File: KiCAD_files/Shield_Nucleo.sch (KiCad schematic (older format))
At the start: 61 parts, among them J1 Shield_nucleo_stage_outline, J2 RJ45_LED_Shielded, J3 RJ45_LED_Shielded, J4 Conn_01x02_Male, J5 Conn_01x04_Male, U1 NUCLEO-F401RE, U2 AT25xxx, U3 TCAN334GDR

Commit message: WIP: added STM32G4 symbol and footprint LQFP64
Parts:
- removed U1: NUCLEO-F401RE, Footprints:ST_NUCLEO-G474, symbol Symbols:NUCLEO-F401RE
- added U?: STM32G474RE, Package_QFP:LQFP-64_10x10mm_P0.5mm, symbol Symbols:STM32G474RE
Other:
- moved on the sheet: J4, J5, TP1, TP10, TP11, TP4, TP5, TP6, TP7, TP8, TP9

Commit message: WIP: nearly finished composant placement
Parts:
- removed J1: Shield_nucleo_stage_outline, Footprints:Shield_nucleo_outline, symbol Symbols:Shield_nucleo_stage_outline
- removed U?: STM32G474RE, Package_QFP:LQFP-64_10x10mm_P0.5mm, symbol Symbols:STM32G474RE
- added C10, C11, C13, C20, C21, C22, C25, C26, C30, C31, C32, C5, C7, C8, C9: 100nF, Capacitor_SMD:C_0805_2012Metric, symbol Device:C_Small
- added C12: 1µF, Capacitor_SMD:C_0805_2012Metric, symbol Device:C_Small
- added C14: 10nF, Capacitor_SMD:C_0805_2012Metric, symbol Device:C_Small
- added C15, C16: CP1_Small, symbol Device:CP1_Small
- added C17, C18, C27, C28: 33pF, Capacitor_SMD:C_0805_2012Metric, symbol Device:C_Small
- added C23, C33: 1uF, Capacitor_SMD:C_0805_2012Metric, symbol Device:C_Small
- added C24, C34: 10uF, Capacitor_SMD:C_1210_3225Metric, symbol Device:C_Small
- added C3, C4: 12pF, Capacitor_SMD:C_0805_2012Metric, symbol Device:C_Small
- added C6: 4,7uF, Capacitor_SMD:C_0805_2012Metric, symbol Device:C_Small
- added D10, D11: STTH4R02U, Diode_SMD:D_SMB, symbol Device:D_Schottky
- added D3, D4, D5, D6, D7, D8, D9: 3.3V, Diode_SMD:D_SOD-123, symbol Device:D_Zener_Small
- added FB1: Ferrite_Bead_Small, Resistor_SMD:R_0805_2012Metric, symbol Device:Ferrite_Bead_Small
- added J1, J6: Conn_01x02, symbol Connector_Generic:Conn_01x02
- added J7: Conn_01x03_Female, symbol Connector:Conn_01x03_Female
- added J?: Conn_02x05_Counter_Clockwise, symbol Connector_Generic:Conn_02x05_Counter_Clockwise
- added PS1: IA0505S, Converter_DCDC:Converter_DCDC_muRata_CRE1xxxxxx3C_THT, symbol Converter_DCDC:IA0505S
- added PS2: IA0512S, Converter_DCDC:Converter_DCDC_muRata_CRE1xxxxxx3C_THT, symbol Converter_DCDC:IA0512S
- added PS4: PQDE6W-Q110-S5-D, Footprints:PQDE6W-Q110-S5-D, symbol Symbols:PQDE6W-Q110-S5-D
- added PS5: VXO78xxx, symbol Symbols:VXO78xxx
- added R14, R17, R18, R21: 51, Resistor_SMD:R_0805_2012Metric, symbol Device:R
- added R15, R19: 20k, Resistor_SMD:R_0805_2012Metric, symbol Device:R
- added R16, R20: 2.2, Resistor_SMD:R_0805_2012Metric, symbol Device:R
- added R22: 1k, Resistor_SMD:R_0805_2012Metric, symbol Device:R
- added R23: 220, Resistor_SMD:R_0805_2012Metric, symbol Device:R
- added SW1: SW_Push, symbol Switch:SW_Push
- added SWD1: Conn_01x06_Female, symbol Connector:Conn_01x06_Female
- added TP16, TP31, TP34, TP35, TP36, TP37, TP38, TP39, TP40, TP41, TP42, TP43, TP44, TP45: TestPoint, TestPoint:TestPoint_Pad_D1.5mm, symbol Connector:TestPoint
- added U1: STM32G474RE, Package_QFP:LQFP-64_10x10mm_P0.5mm, symbol Symbols:STM32G474RE
- added U4: AP1117-33, Package_TO_SOT_SMD:SOT-223-3_TabPin2, symbol Regulator_Linear:AP1117-33
- added U5, U6: UCC21222DR, Package_SO:SOIC-16_4.55x10.3mm_P1.27mm, symbol Driver_FET:UCC21520DW
- added U7: SFH617A-2X009T, Package_DIP:SMDIP-4_W7.62mm, symbol Isolator:SFH617A-2X009T
- added Y1: NX3225SA-16.000000MHZ-T1, Crystal:Crystal_SMD_3225-4Pin_3.2x2.5mm, symbol Device:Crystal_GND24
- R3, R5, R7: value 39k -> 20k
- R9: value 39k -> 51
- TP1, TP10, TP11, TP12, TP13, TP14, TP15, TP17, TP18, TP19, TP2, TP20, TP21, TP22, TP23, TP24, TP25, TP26, TP27, TP28, TP29, TP3, TP30, TP32, TP33, TP4, TP5, TP6, TP7, TP8, TP9: footprint TestPoint:TestPoint_THTPad_D2.0mm_Drill1.0mm -> TestPoint:TestPoint_Pad_D1.5mm
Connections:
- net labels added: +12V, +3.3VA, +5V, +5VD, GNDREF, HSE_IN, HSE_OUT, I1_low_mcu, I1_low_op, I2_low_op, I_high_mcu, I_high_op, N, NRST, Neutral_GND_cmd, PWM_H1, PWM_H2, PWM_L1, PWM_L2, STLINK_RX, STLINK_TX, SWCLK, SWDIO, SWO, SW_Node1, SW_Node2, V1_low_mcu, V1_low_op, V2_low_mcu, V2_low_op, VI_high, V_high_mcu, V_high_op
- net labels removed: E5V
- wire segments 205 -> 492
- no-connect marks 5 -> 7
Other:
- note added: "Decoupling capacitors choosen as per datasheet 5.16 Power supply scheme fig.16\n"
- note added: "MCU protections from analog inputs\n"
- note added: "Only one footprint to be populated depending\nif the converter is powered\nfrom a DAB module or is standalone\n"
- note added: "Power input terminals for MCU\nand power side\n"
- note added: "STM32G474RE LQFP64\nPin Mapping"
- note added: "SWD connector\n"
- note added: "Temperature sensor is wired\nto a flexible temp probe \nattached to the heatsink\n"
- note added: "Zener diodes protect from potential overvoltages while resistors prevent accidental high current flow\n\n"
- note removed: "NUCLEO-G474RE Pin Mapping"
- note removed: "Precision divider to adapt 5V signals to 3,3V."
- note removed: "Signal acquisition from power converter"
- moved on the sheet: BT1, C1, C2, D1, D2, F1, F2, J2, J3, J4, J5, JP1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

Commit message: WIP: Added power 3D footprint, placed the feeder, the MCU Remapping differential to single ended to be done and ready to route
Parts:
- removed J7: Conn_01x03_Female, symbol Connector:Conn_01x03_Female
- removed J?: Conn_02x05_Counter_Clockwise, symbol Connector_Generic:Conn_02x05_Counter_Clockwise
- added 3D1: 3D_Footprint, Footprints:3D_Footprint_Power, symbol Symbols:3D_Footprint
- added J8: Conn_02x07_Odd_Even, Connector_PinHeader_1.27mm:PinHeader_2x07_P1.27mm_Vertical_SMD, symbol Connector_Generic:Conn_02x07_Odd_Even
- added R24: 100, Resistor_SMD:R_0805_2012Metric, symbol Device:R
- added R25: 20k, Resistor_SMD:R_0805_2012Metric, symbol Device:R
- added TH1: NXFT15XH103FA2B100, Connector_PinHeader_1.27mm:PinHeader_1x02_P1.27mm_Horizontal, symbol Device:Thermistor
- added TP46, TP47: TestPoint, TestPoint:TestPoint_Pad_D1.5mm, symbol Connector:TestPoint
- C15, C16: footprint (none) -> Capacitor_SMD:CP_Elec_6.3x7.7
- J1, J6: footprint (none) -> Footprints:PTSM-0,5-2-HH0-SMD
- J2, J3: footprint Connector_RJ:RJ45_Amphenol_RJHSE538X -> Footprints:ethernet_RJE721881411
- PS5: footprint (none) -> Footprints:CONV_VXO78012-500-M
- SW1: footprint (none) -> Button_Switch_SMD:SW_Push_1P1T_NO_CK_KMR2
- SWD1: footprint (none) -> Connector_PinHeader_2.54mm:PinHeader_1x06_P2.54mm_Vertical
- U5, U6: footprint Package_SO:SOIC-16_4.55x10.3mm_P1.27mm -> Footprints:SOIC-16_3.9x9.9mm_P1.27mm
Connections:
- wire segments 492 -> 501
- no-connect marks 7 -> 9
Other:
- note added: "B = 3450\n"
- note added: "Max current flowing 0.12mA\n"
- note added: "R = R0 * expB(1/T-1/T0)"
- note added: "R0 = 10kOhm"
- note added: "RJE721881411"
- note added: "RS3-21001D1A"
- note added: "STDC14 / ARM10 connector for debugger connection\nCompatible with STLINKV3\n"
- moved on the sheet: C16, C25, C26, C27, C28, C30, C31, C32, C33, C34, D11, J4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

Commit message: WIP: Added pin positions in power footprint Mapped single ended adc on STM32, added feeder filter
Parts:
- added C19, C35, C36, C37, C38, C39, C40: 10uF, Capacitor_SMD:C_1210_3225Metric, symbol Device:C_Small
- added C29: 10 to 47uF, Capacitor_SMD:CP_Elec_8x11.9, symbol Device:CP1_Small
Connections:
- net labels added: I2_low_mcu, Temp_mcu
- net labels removed: I1_low, I2_low, I_high, V1_low_N, V1_low_P, V2_low_N, V2_low_P, V_high_N, V_high_P
- wire segments 501 -> 537
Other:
- note added: "filter to be added\n"
- moved on the sheet: C11, C13, C17, C18, C20, C21, C22, C23, C24, C25, C26, C27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

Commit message: WIP: nearly finished routing - Power need via stiching Signal miss test points connections.
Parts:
- removed 3D1: 3D_Footprint, Footprints:3D_Footprint_Power, symbol Symbols:3D_Footprint
- removed TP10, TP11, TP16, TP17, TP18, TP19, TP20, TP21, TP22, TP23, TP24, TP25, TP26, TP27, TP28, TP29, TP30, TP31, TP34, TP35, TP36, TP37, TP38, TP39, TP40, TP41, TP42, TP43, TP44, TP45, TP46, TP47, TP9: TestPoint, TestPoint:TestPoint_Pad_D1.5mm, symbol Connector:TestPoint
- added J7: Power, Footprints:3D_Footprint_Power, symbol Symbols:Power
- added JP3, JP4: SolderJumper_2_Open, Jumper:SolderJumper-2_P1.3mm_Open_Pad1.0x1.5mm, symbol Jumper:SolderJumper_2_Open
- added LED1: LED, LED_SMD:LED_0805_2012Metric, symbol Device:LED
- added R26, R27: 100K, Resistor_SMD:R_0805_2012Metric, symbol Device:R_Small
- added R28: 330, Resistor_SMD:R_0805_2012Metric, symbol Device:R
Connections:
- net labels added: +12VD, DAC2, LED_BUILTIN, VREF1024, VREF2048
- net labels removed: HRTIM1_CHC1, HRTIM1_CHC2, HRTIM1_CHD1, HRTIM1_CHD2, HRTIM1_CHE1, HRTIM1_CHE2, HRTIM1_CHF1, HRTIM1_CHF2
- wire segments 537 -> 571
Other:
- note added: "Two ways of having a 1.024V VREF signal\n- a stupid hardware based one \n- a DAC based solutions that needs to \nwork on the software side\n"
- note added: "VREF2048 comes from the STM32G474 internal reference. \nIt has to be configured through VREFBUF register."
- moved on the sheet: C11, C13, C15, C16, C17, C18, C19, C20, C21, C22, C23, C24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

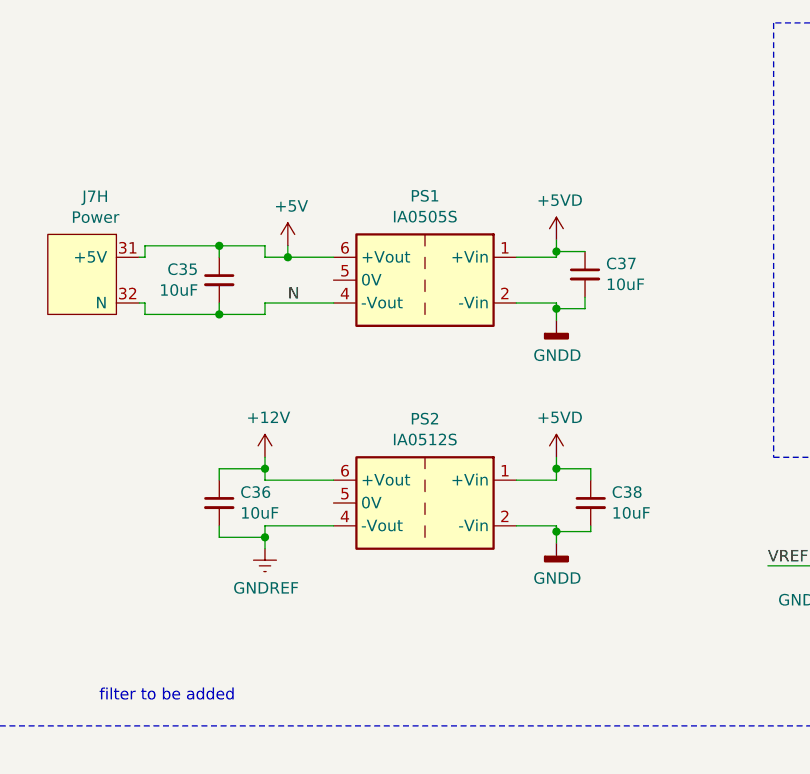
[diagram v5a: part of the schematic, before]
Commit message: WIP: First nightly version of V1.1 - Need verification and validation Possible issue with a current loop on the power PCB...
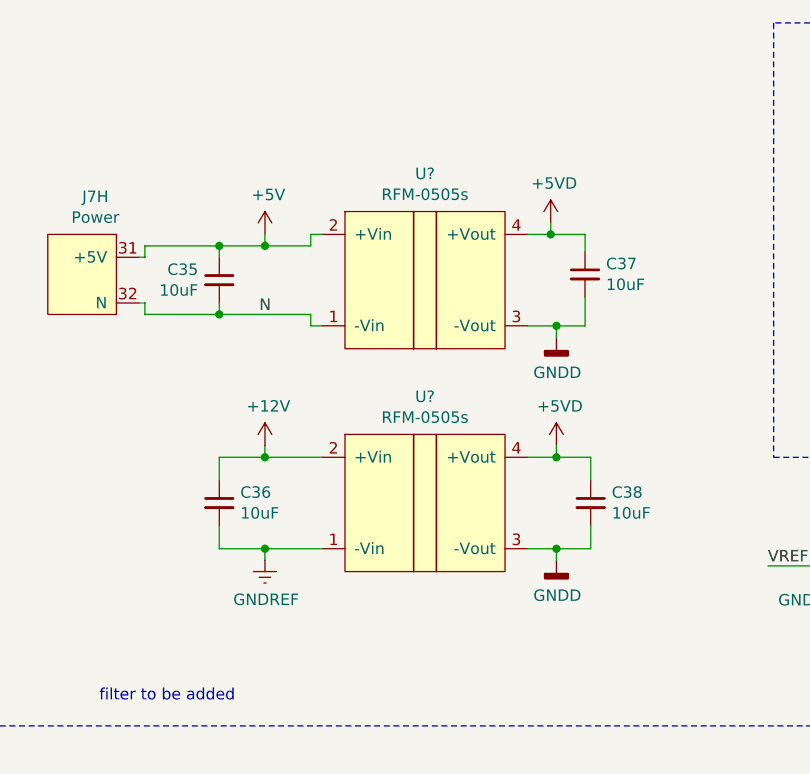
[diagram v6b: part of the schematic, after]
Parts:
- removed PS1: IA0505S, Converter_DCDC:Converter_DCDC_muRata_CRE1xxxxxx3C_THT, symbol Converter_DCDC:IA0505S
- removed PS2: IA0512S, Converter_DCDC:Converter_DCDC_muRata_CRE1xxxxxx3C_THT, symbol Converter_DCDC:IA0512S
- added U? (x2): RFM-0505s, Converter_DCDC:Converter_DCDC_muRata_CRE1xxxxxx3C_THT, symbol Symbols:RFM-0505s
- TP1, TP12, TP13, TP14, TP15, TP2, TP3, TP32, TP33, TP4, TP5, TP6, TP7, TP8: footprint TestPoint:TestPoint_Pad_D1.5mm -> TestPoint:TestPoint_THTPad_D2.0mm_Drill1.0mm
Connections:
- net +12V: now also U?.2 (+Vin)
- net +5V: now also U?.2 (+Vin)
- net +5VD: now also U?.4 (+Vout), U?.4 (+Vout)
- net GNDD: now also U?.3 (-Vout), U?.3 (-Vout)
- net GNDREF: now also U?.1 (-Vin)
- net N: now also U?.1 (-Vin)

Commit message: saved file
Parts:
- gave numbers to parts that had none: 2
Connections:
- net +12V: now also U9.4 (+Vout); no longer U9.2 (+Vin)
- net +5V: now also U8.4 (+Vout); no longer U8.2 (+Vin)
- net +5VD: now also U8.2 (+Vin), U9.2 (+Vin); no longer U8.4 (+Vout), U9.4 (+Vout)
- net GNDD: now also U8.1 (-Vin), U9.1 (-Vin); no longer U8.3 (-Vout), U9.3 (-Vout)
- net GNDREF: now also U9.3 (-Vout); no longer U9.1 (-Vin)
- net N: now also U8.3 (-Vout); no longer U8.1 (-Vin)
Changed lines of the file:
@@
 	6125 3800 8750 3800
 $Comp
-L Symbols:RFM-0505s U?
+L Symbols:RFM-0505s U8
 U 1 1 60E32218
 P 14600 8375
-F 0 "U?" H 14600 8840 50  0000 C CNN
+F 0 "U8" H 14600 8840 50  0000 C CNN
 F 1 "RFM-0505s" H 14600 8749 50  0000 C CNN
 F 2 "Converter_DCDC:Converter_DCDC_muRata_CRE1xxxxxx3C_THT" H 14600 8725 50  0001 C CNN
 F 3 "" H 14600 8725 50  0001 C CNN
 	1    14600 8375
-	1    0    0    -1
+	-1   0    0    -1
 $EndComp
 Wire Wire Line
@@
 	13900 8225 14100 8225
 $Comp
-L Symbols:RFM-0505s U?
+L Symbols:RFM-0505s U9
 U 1 1 6145CAC6
 P 14600 9350
-F 0 "U?" H 14600 9815 50  0000 C CNN
+F 0 "U9" H 14600 9815 50  0000 C CNN
 F 1 "RFM-0505s" H 14600 9724 50  0000 C CNN
 F 2 "Converter_DCDC:Converter_DCDC_muRata_CRE1xxxxxx3C_THT" H 14600 9700 50  0001 C CNN
 F 3 "" H 14600 9700 50  0001 C CNN
 	1    14600 9350
-	1    0    0    -1
+	-1   0    0    -1
 $EndComp
 Wire Wire Line

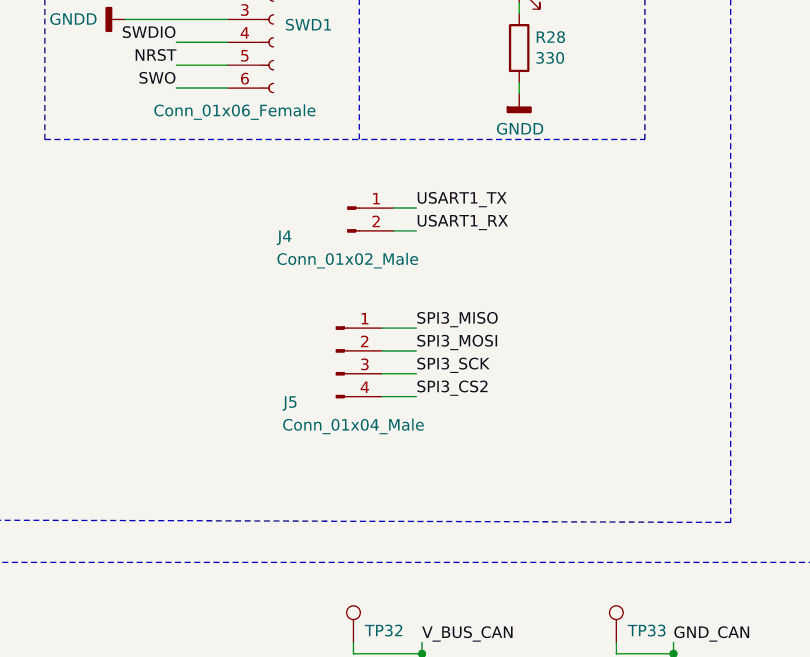
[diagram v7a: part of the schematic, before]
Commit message: WIP: Corrected small plane mistakes, added GNDREF pin to ext USART and SPI.
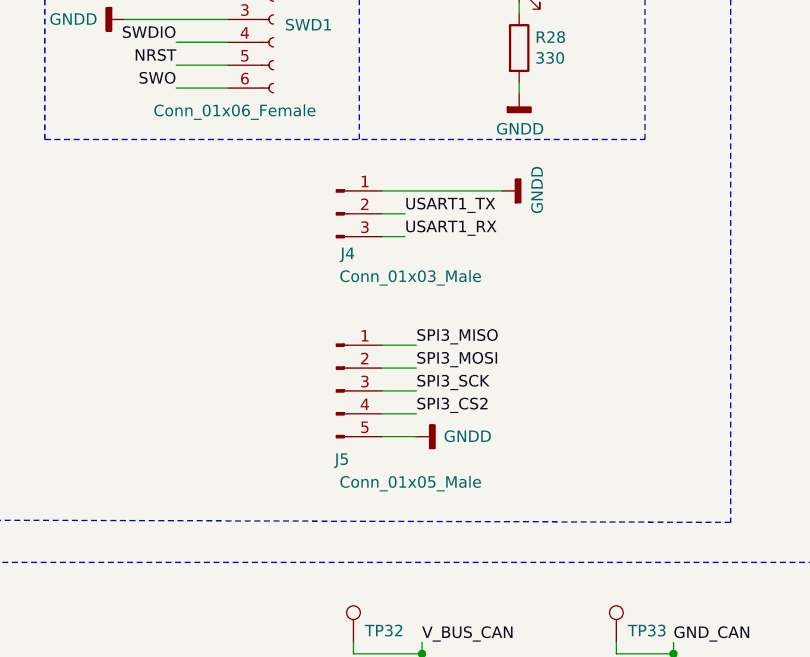
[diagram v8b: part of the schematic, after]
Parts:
- removed J4: Conn_01x02_Male, Connector_PinHeader_2.54mm:PinHeader_1x02_P2.54mm_Vertical, symbol Connector:Conn_01x02_Male
- removed J5: Conn_01x04_Male, Connector_PinHeader_2.54mm:PinHeader_1x04_P2.54mm_Vertical, symbol Connector:Conn_01x04_Male
- added J4: Conn_01x03_Male, Connector_PinHeader_2.54mm:PinHeader_1x03_P2.54mm_Vertical, symbol Connector:Conn_01x03_Male
- added J5: Conn_01x05_Male, Connector_PinHeader_2.54mm:PinHeader_1x05_P2.54mm_Vertical, symbol Connector:Conn_01x05_Male
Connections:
- net GNDD: now also J4.1 (Pin_1), J5.5 (Pin_5)
- net SPI3_CS2: now also J5.4 (Pin_4)
- net SPI3_MISO: now also J5.1 (Pin_1)
- net SPI3_MOSI: now also J5.2 (Pin_2)
- net SPI3_SCK: now also J5.3 (Pin_3)
- net USART1_RX: now also J4.3 (Pin_3)
- net USART1_TX: now also J4.2 (Pin_2)
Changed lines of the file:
@@
 Wire Wire Line
 	7475 7075 7475 7125
-$Comp
-L Connector:Conn_01x04_Male J5
-U 1 1 605189A2
-P 7400 5800
-F 0 "J5" H 7200 5575 50  0000 C CNN
-F 1 "Conn_01x04_Male" H 7475 5475 50  0000 C CNN
-F 2 "Connector_PinHeader_2.54mm:PinHeader_1x04_P2.54mm_Vertical" H 7400 5800 50  0001 C CNN
-F 3 "~" H 7400 5800 50  0001 C CNN
-	1    7400 5800
-	1    0    0    -1
-$EndComp
-$Comp
-L Connector:Conn_01x02_Male J4
-U 1 1 6051B580
-P 7450 5175
-F 0 "J4" H 7175 5050 50  0000 C CNN
-F 1 "Conn_01x02_Male" H 7450 4950 50  0000 C CNN
-F 2 "Connector_PinHeader_2.54mm:PinHeader_1x02_P2.54mm_Vertical" H 7450 5175 50  0001 C CNN
-F 3 "~" H 7450 5175 50  0001 C CNN
-	1    7450 5175
-	1    0    0    -1
-$EndComp
-Text Label 7750 5175 0    50   ~ 0
+Text Label 7700 5200 0    50   ~ 0
 USART1_TX
 Wire Wire Line
-	7750 5175 7650 5175
-Text Label 7750 5275 0    50   ~ 0
+	7700 5200 7600 5200
+Text Label 7700 5300 0    50   ~ 0
 USART1_RX
 Wire Wire Line
-	7750 5275 7650 5275
-Text Label 7750 5800 0    50   ~ 0
+	7700 5300 7600 5300
+Text Label 7750 5875 0    50   ~ 0
 SPI3_MOSI
-Text Label 7750 5700 0    50   ~ 0
+Text Label 7750 5775 0    50   ~ 0
 SPI3_MISO
-Text Label 7750 5900 0    50   ~ 0
+Text Label 7750 5975 0    50   ~ 0
 SPI3_SCK
 Wire Wire Line
-	7750 5900 7600 5900
+	7750 5975 7600 5975
 Text Label 5025 2675 2    50   ~ 0
 SPI3_CS
-Text Label 7750 6000 0    50   ~ 0
+Text Label 7750 6075 0    50   ~ 0
 SPI3_CS2
 Wire Wire Line
-	7750 6000 7600 6000
+	7750 6075 7600 6075
 Wire Wire Line
-	7750 5800 7600 5800
+	7750 5875 7600 5875
 Wire Wire Line
-	7750 5700 7600 5700
+	7750 5775 7600 5775
 Text Label 2450 4275 0    50   ~ 0
 SPI3_CS2
@@
 Wire Wire Line
 	13900 9150 14150 9150
+$Comp
+L Connector:Conn_01x03_Male J4
+U 1 1 607EEA57
+P 7400 5200
+F 0 "J4" H 7450 5025 50  0000 C CNN
+F 1 "Conn_01x03_Male" H 7725 4925 50  0000 C CNN
+F 2 "Connector_PinHeader_2.54mm:PinHeader_1x03_P2.54mm_Vertical" H 7400 5200 50  0001 C CNN
+F 3 "~" H 7400 5200 50  0001 C CNN
+	1    7400 5200
+	1    0    0    -1
+$EndComp
+$Comp
+L power:GNDD #PWR044
+U 1 1 608E5E39
+P 8125 5100
+F 0 "#PWR044" H 8125 4850 50  0001 C CNN
+F 1 "GNDD" H 8129 4945 50  0000 C CNN
+F 2 "" H 8125 5100 50  0001 C CNN
+F 3 "" H 8125 5100 50  0001 C CNN
+	1    8125 5100
+	0    -1   -1   0
+$EndComp
+Wire Wire Line
+	7600 5100 8125 5100
+$Comp
+L Connector:Conn_01x05_Male J5
+U 1 1 609DAEDF
+P 7400 5975
+F 0 "J5" H 7425 5675 50  0000 C CNN
+F 1 "Conn_01x05_Male" H 7725 5575 50  0000 C CNN
+F 2 "Connector_PinHeader_2.54mm:PinHeader_1x05_P2.54mm_Vertical" H 7400 5975 50  0001 C CNN
+F 3 "~" H 7400 5975 50  0001 C CNN
+	1    7400 5975
+	1    0    0    -1
+$EndComp
+$Comp
+L power:GNDD #PWR043
+U 1 1 60A7F5F6
+P 7750 6175
+F 0 "#PWR043" H 7750 5925 50  0001 C CNN
+F 1 "GNDD" V 7750 5950 50  0000 C CNN
+F 2 "" H 7750 6175 50  0001 C CNN
+F 3 "" H 7750 6175 50  0001 C CNN
+	1    7750 6175
+	0    -1   -1   0
+$EndComp
+Wire Wire Line
+	7600 6175 7750 6175
 $EndSCHEMATC
